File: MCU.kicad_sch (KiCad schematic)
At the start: 16 parts, among them J10 SWD, J11 UART, J12 I2C1, U12 STM32F030C8Tx

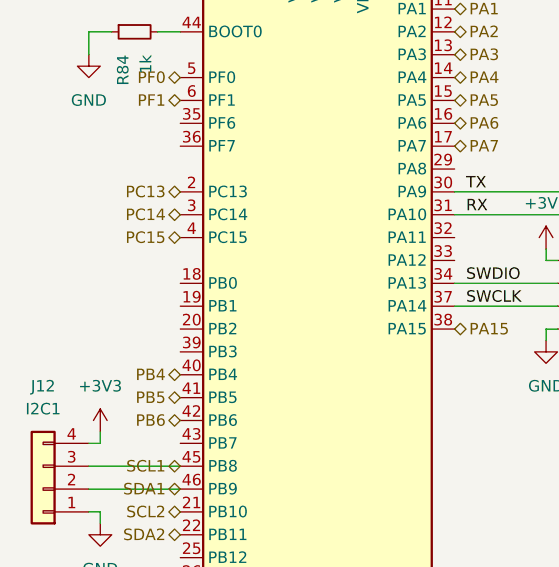
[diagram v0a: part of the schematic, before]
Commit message: Add external board detect pin to MCU
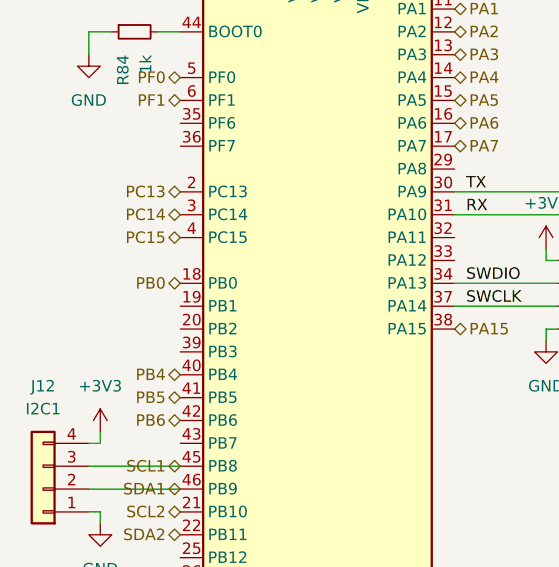
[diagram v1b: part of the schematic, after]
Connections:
- net PB0: now reaches U12.18 (PB0)
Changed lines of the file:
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@@
+		)
+	)
+	(hierarchical_label "PB0"
+		(shape bidirectional)
+		(at 40.64 73.66 180)
+		(fields_autoplaced yes)
+		(effects
+			(font
+				(size 1.27 1.27)
+			)
+			(justify right)
 		)
 	)

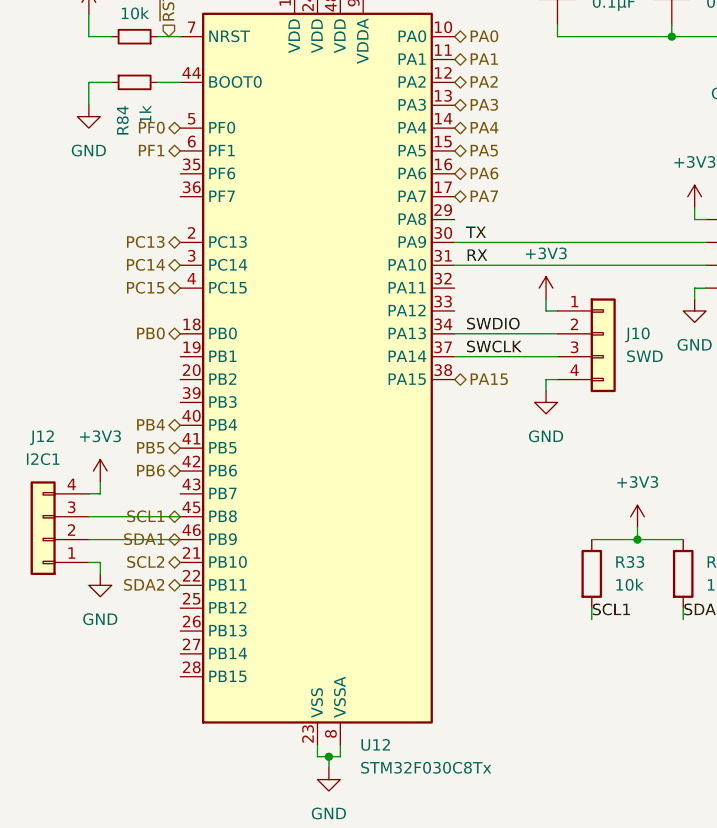
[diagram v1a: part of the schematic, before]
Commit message: pcb: replaced 20P slot with mirrored connector
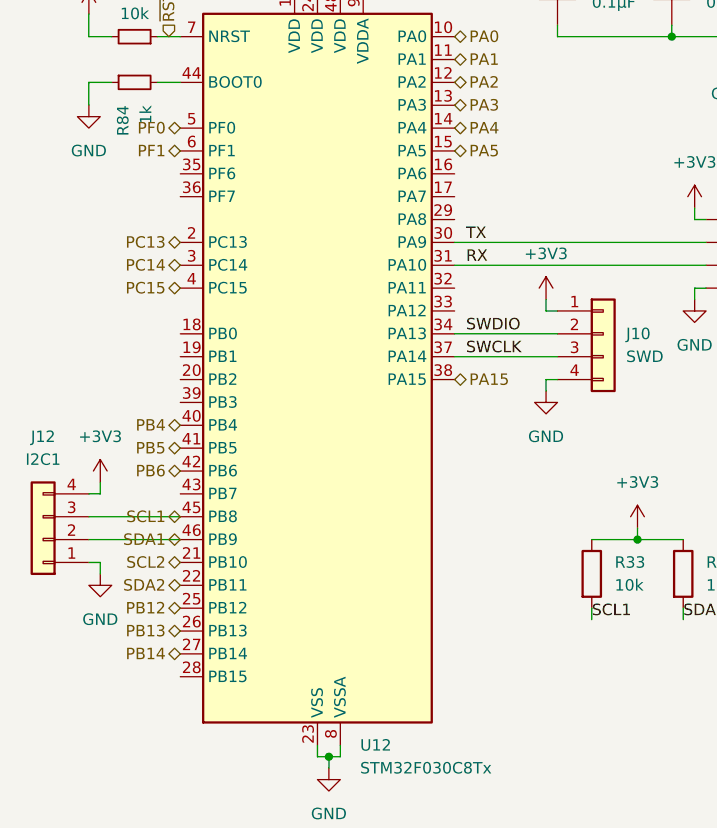
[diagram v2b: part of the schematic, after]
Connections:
- net PB12: now reaches U12.25 (PB12)
- net PB13: now reaches U12.26 (PB13)
- net PB14: now reaches U12.27 (PB14)
- net PA6: no longer names the net of U12.16 (PA6)
- net PA7: no longer names the net of U12.17 (PA7)
- net PB0: no longer names the net of U12.18 (PB0)
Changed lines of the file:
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@@
+		)
+	)
+	(hierarchical_label "PB12"
+		(shape bidirectional)
+		(at 40.64 104.14 180)
+		(fields_autoplaced yes)
+		(effects
+			(font
+				(size 1.27 1.27)
+			)
+			(justify right)
 		)
 	)
@@
 		)
 	)
+	(hierarchical_label "PB14"
+		(shape bidirectional)
+		(at 40.64 109.22 180)
+		(fields_autoplaced yes)
+		(effects
+			(font
+				(size 1.27 1.27)
+			)
+			(justify right)
+		)
+	)
 	(hierarchical_label "PB5"
 		(shape bidirectional)
@@
 		)
 	)
-	(hierarchical_label "PA7"
-		(shape bidirectional)
-		(at 71.12 58.42 0)
-		(fields_autoplaced yes)
-		(effects
-			(font
-				(size 1.27 1.27)
-			)
-			(justify left)
+	(hierarchical_label "PB13"
+		(shape bidirectional)
+		(at 40.64 106.68 180)
+		(fields_autoplaced yes)
+		(effects
+			(font
+				(size 1.27 1.27)
+			)
+			(justify right)
 		)
 	)
@@
 		)
 	)
-	(hierarchical_label "PA6"
-		(shape bidirectional)
-		(at 71.12 55.88 0)
-		(fields_autoplaced yes)
-		(effects
-			(font
-				(size 1.27 1.27)
-			)
-			(justify left)
-		)
-	)
 	(hierarchical_label "PF1"
 		(shape bidirectional)
@@
 		(fields_autoplaced yes)
 		(effects
-			(font
-				(size 1.27 1.27)
-			)
-			(justify right)
-		)
-	)
-	(hierarchical_label "PB0"
-		(shape bidirectional)
-		(at 40.64 73.66 180)
-		(fields_autoplaced yes)
-		(effects

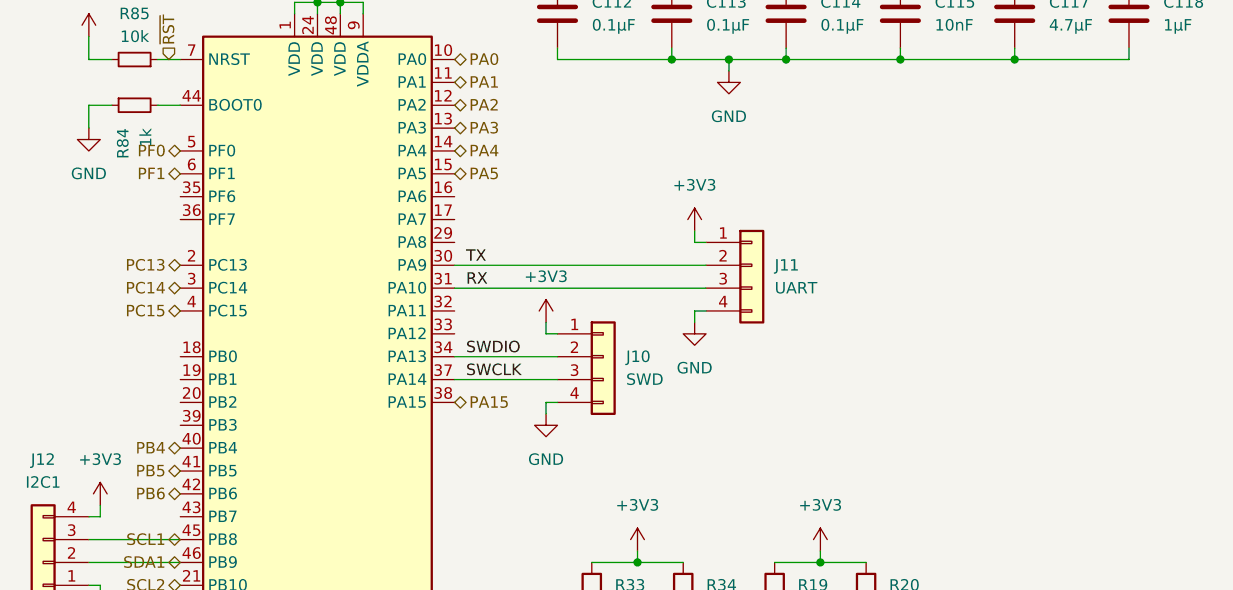
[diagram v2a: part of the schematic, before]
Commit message: pcb: add 12V PCIe power converters
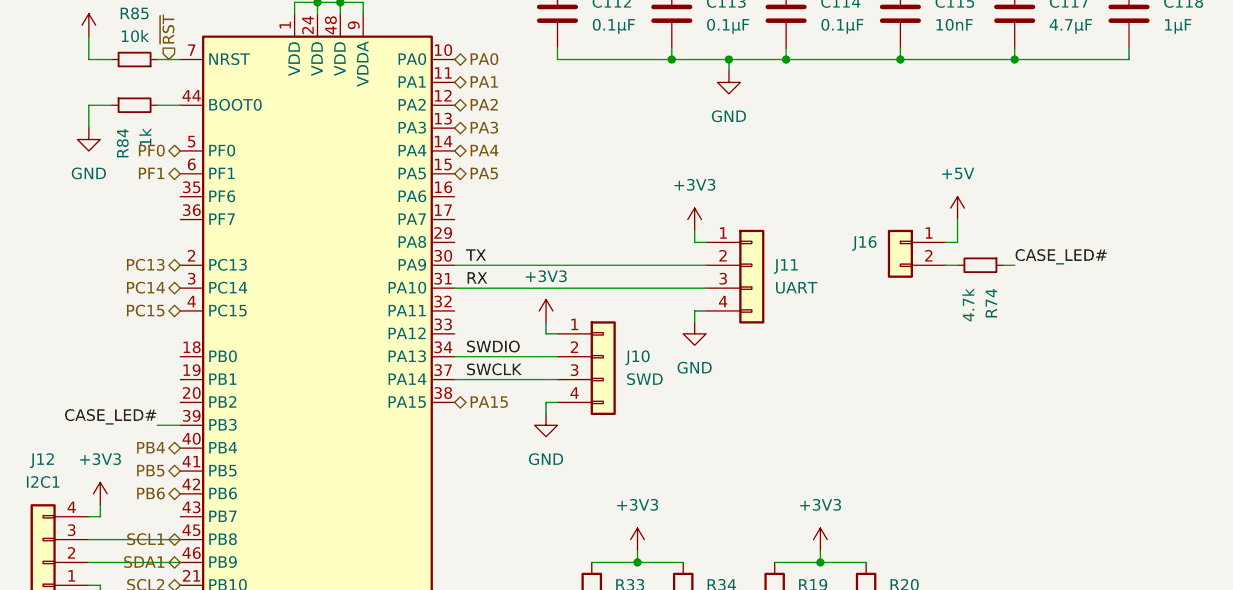
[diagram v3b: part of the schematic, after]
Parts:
- added J16: ~, Connector_JST:JST_PH_S2B-PH-K_1x02_P2.00mm_Horizontal, symbol Connector_Generic:Conn_01x02
- added R74: 4.7k, Resistor_SMD:R_0402_1005Metric, symbol Device:R_Small
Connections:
- net CASE_LED#: now reaches U12.39 (PB3)
- net CASE_LED#: now also R74.1
- new net: J16.2 (Pin_2), R74.2
- new net +5V: J16.1 (Pin_1)

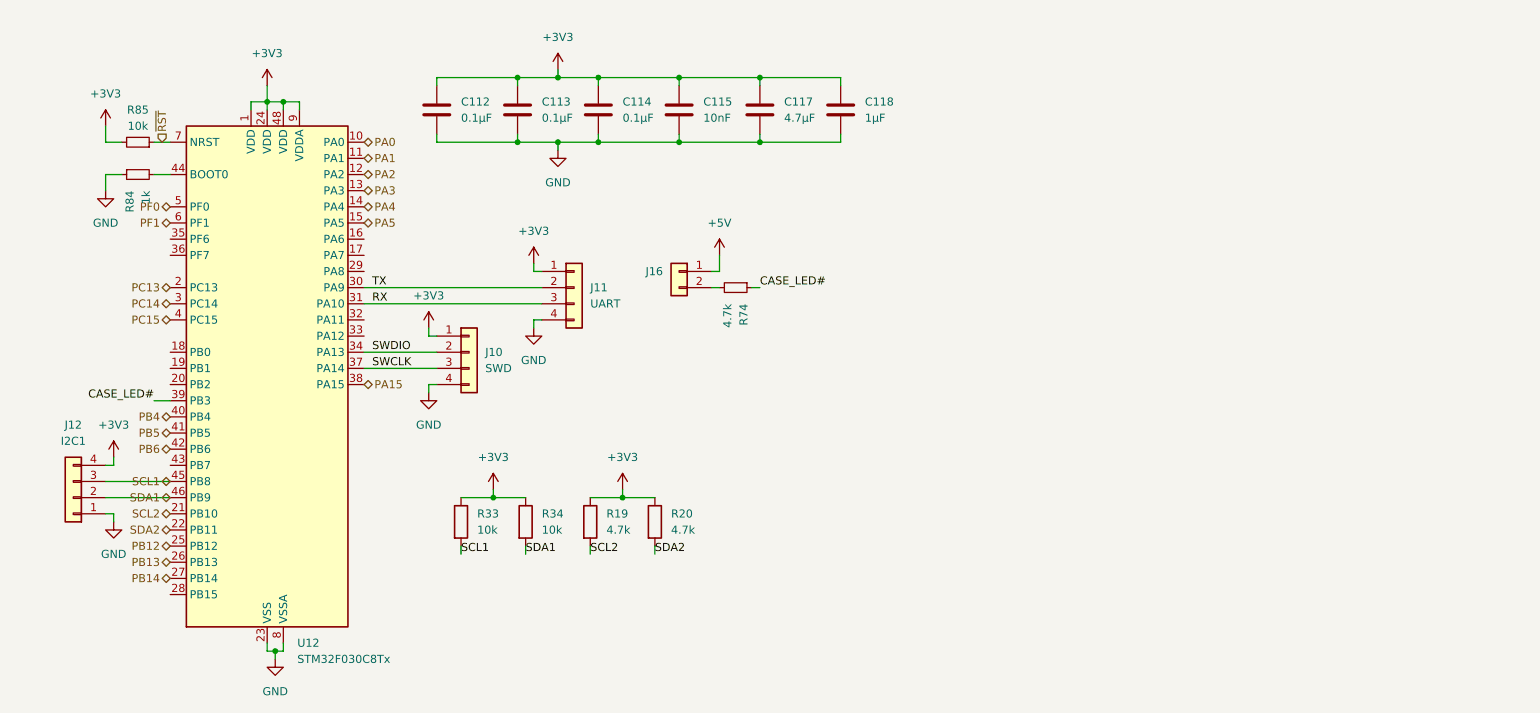
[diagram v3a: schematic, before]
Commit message: pcb: added fans and thermistor to standard pcb
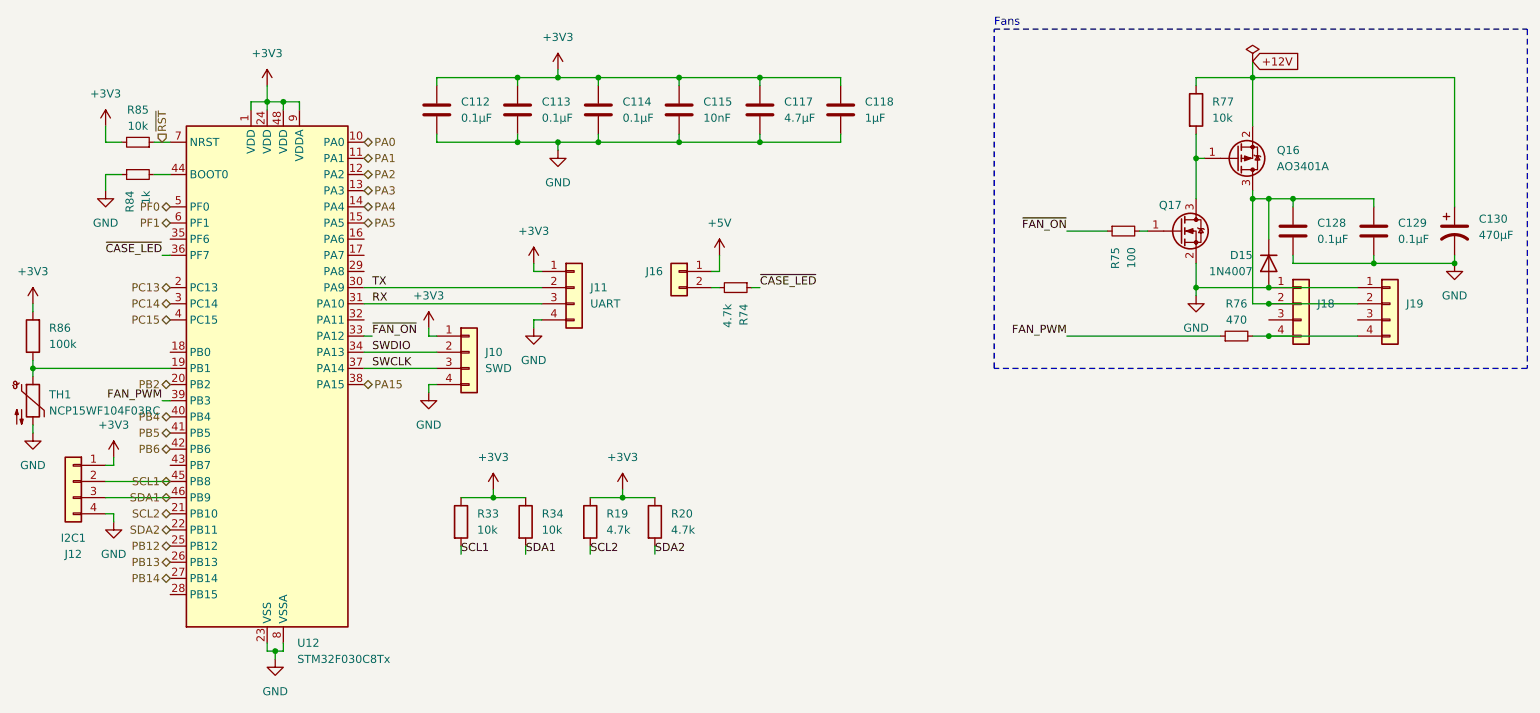
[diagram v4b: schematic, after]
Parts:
- added C128, C129: 0.1µF, Capacitor_SMD:C_0603_1608Metric, symbol Device:C
- added C130: 470µF, Capacitor_THT:CP_Radial_D10.0mm_P5.00mm, symbol Device:C_Polarized_US
- added D15: 1N4007, Diode_SMD:D_SOD-123F, symbol Diode:1N4007
- added J18, J19: ~, 470531000:CONN_SD-47053-001_H10p00_MOL, symbol Connector_Generic:Conn_01x04
- added Q16: AO3401A, Package_TO_SOT_SMD:SOT-23, symbol Transistor_FET:AO3401A
- added Q17: 2N7002W, 2N7002W:SOT-323-3_L2.0-W1.3-P1.30-LS2.1-BR, symbol Transistor_FET:BSS214NW
- added R75: 100, Resistor_SMD:R_0402_1005Metric, symbol Device:R_Small
- added R76: 470, Resistor_SMD:R_0402_1005Metric, symbol Device:R_Small
- added R77: 10k, Resistor_SMD:R_0402_1005Metric, symbol Device:R
- added R86: 100k, Resistor_SMD:R_0402_1005Metric, symbol Device:R
- added TH1: NCP15WF104F03RC, Resistor_SMD:R_0402_1005Metric, symbol Device:Thermistor_NTC
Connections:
- net +3V3: now also J12.1 (Pin_1), R86.2; no longer J12.4 (Pin_4)
- net GND: now also J12.4 (Pin_4), C128.2, C129.2, C130.2, D15.2 (A), J18.1 (Pin_1), J19.1 (Pin_1), Q17.2 (S), TH1.2; no longer J12.1 (Pin_1)
- net SCL1: now also J12.2 (Pin_2); no longer J12.3 (Pin_3)
- net SDA1: now also J12.3 (Pin_3); no longer J12.2 (Pin_2)
- net at U12.19 (PB1): now also R86.1, TH1.1
- net PB2: now reaches U12.20 (PB2)
- net ~{FAN_ON}: now reaches U12.33 (PA12)
- net ~{FAN_ON}: now also R75.1
- net ~{CASE_LED}: now reaches U12.36 (PF7)
- net ~{CASE_LED}: now also R74.1
- net CASE_LED# renamed FAN_PWM
- net FAN_PWM: now also R76.1; no longer R74.1
- new net: J18.4 (Pin_4), J19.4 (Pin_4), R76.2
- new net: C128.1, C129.1, D15.1 (K), J18.2 (Pin_2), J19.2 (Pin_2), Q16.3 (D)
- new net: Q17.1 (G), R75.2
- new net: Q16.1 (G), Q17.3 (D), R77.2
- new net +12V: C130.1, Q16.2 (S), R77.1
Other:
- note added: "Fans"
- moved on the sheet: J12

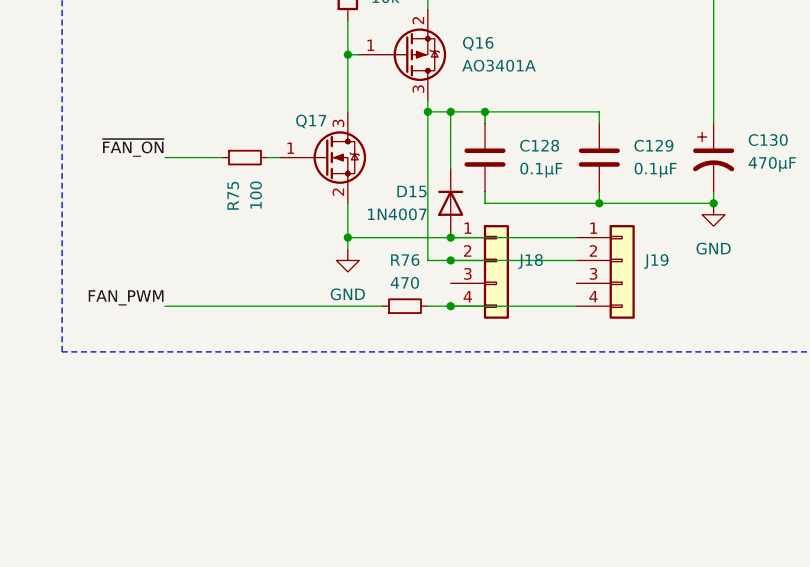
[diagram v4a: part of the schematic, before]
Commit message: pcb: reduced gate resistor in schematic review
Also updated some missing attributes.
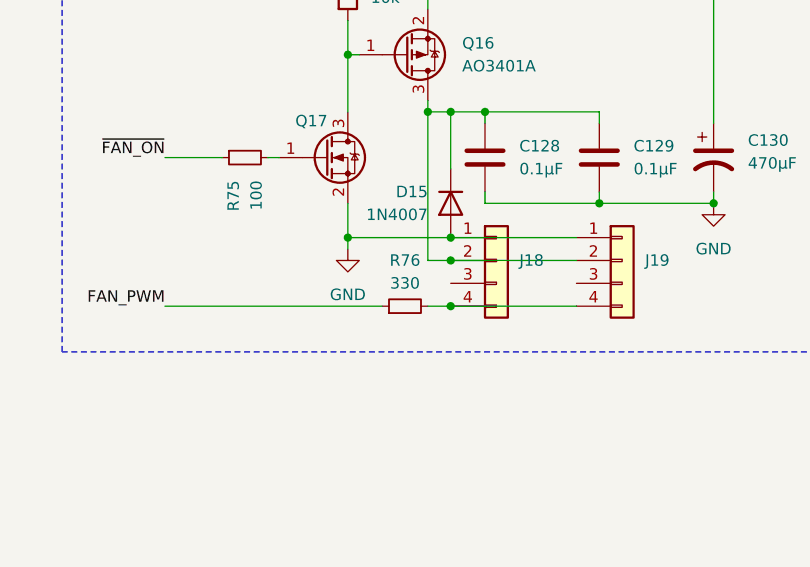
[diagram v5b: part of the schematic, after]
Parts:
- Q16: LCSC (none) -> C15127; Part_Number (none) -> AO3401A
- R76: value 470 -> 330; LCSC C25117 -> C25104; Part_Number 0402WGF4700TCE -> 0402WGF3300TCE
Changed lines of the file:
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@@
 			)
 		)
-		(property "Value" "470"
+		(property "Value" "330"
 			(at 208.28 68.58 90)
 			(effects
@@
 			)
 		)
-		(property "Part_Number" "0402WGF4700TCE"
+		(property "Part_Number" "0402WGF3300TCE"
 			(at 208.28 71.12 0)
 			(effects
@@
 			)
 		)
-		(property "LCSC" "C25117"
+		(property "LCSC" "C25104"
 			(at 208.28 71.12 0)
 			(effects
@@
 			(at 208.28 43.18 0)
 			(effects
+				(font
+					(size 1.27 1.27)
+				)
+				(hide yes)
+			)
+		)
+		(property "Part_Number" "AO3401A"
+			(at 208.28 43.18 0)
+			(effects
+				(font
+					(size 1.27 1.27)
+				)
+				(hide yes)
+			)
+		)
+		(property "LCSC" "C15127"
+			(at 208.28 43.18 0)
+			(effects
